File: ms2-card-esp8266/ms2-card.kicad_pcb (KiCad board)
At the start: 2 copper layers, 100 x 54 mm, 58 parts, among them J1 Schaltregler, J10 MicroSD_SPI_CD, J11 Conn_01x06, J2 ESP Prog, J20 Smartcard Connector, J21 PogoPin, J22 Card Edge, J23 Conn_01x04, J30 USB_B_Micro, J31 Power Select, J32 Conn_01x03, Q1 MMBT3904, Q2 MMBT3904, SW1 RESET, U1 ESP-12F, U2 FM24C64B, U20 BL1551B, U3 BL1551B, U30 CP2102N-Axx-xQFN24, U4 BL1551B, U6 AMS1117-3.3

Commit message: wip
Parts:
- moved D32 3.77 mm to (185.3, 151.8)
- moved R32 3.77 mm to (185.3, 150.1)
- moved D31 2.85 mm to (182.0, 151.8)
- moved R31 2.85 mm to (182.0, 150.1)
- moved R21 1.28 mm to (179.2, 138.5)
- moved R20 1.15 mm to (181.0, 138.5)
- turned D1 to 180 degrees
- turned R4 to 180 degrees
- turned R3 to 180 degrees
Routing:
- net VCC: track 0.00 -> 82.6 mm, vias 0 -> 2
- net /VBUS: track 14.3 -> 72.7 mm, vias 2 -> 3
- net Net-(J20-Pad4): track 0.00 -> 55.8 mm
- net Net-(J20-Pad5): track 0.00 -> 49.1 mm
- net /CS: track 0.00 -> 43.5 mm
- net /RxD: track 0.00 -> 38.3 mm
- net /TxD: track 0.00 -> 36.6 mm
- net /nRST: track 0.00 -> 29.7 mm, vias 0 -> 1
- net /MOSI: track 0.00 -> 29.4 mm
- net +5V: track 0.00 -> 25.6 mm, vias 0 -> 1
- net /RTS: track 0.00 -> 14.7 mm
- net /DTR: track 0.00 -> 14.1 mm, vias 0 -> 2
- net /CLK: track 0.00 -> 12.4 mm, vias 0 -> 2
- net /MISO: track 0.00 -> 10.5 mm
- net /LED: track 0.00 -> 8.85 mm
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
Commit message: in production
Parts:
- moved J23 0.14 mm to (160.4, 113.0)
- moved C2 0.11 mm to (167.1, 139.5)
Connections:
- U1 pad 22: unconnected-(U1-Pad22) -> /Card
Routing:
- net /CSCL: track 0.00 -> 96.5 mm, vias 0 -> 5
- net VCC: track 82.6 -> 170.5 mm, vias 2 -> 3
- net Net-(J22-Pad1): track 0.00 -> 81.3 mm
- net Net-(J20-Pad2): track 0.00 -> 73.6 mm
- net /CSDA: track 0.00 -> 68.9 mm, vias 0 -> 4
- net /MS2PWR: track 0.00 -> 65.0 mm
- net /PP: track 0.00 -> 61.3 mm, vias 0 -> 1
- net Net-(J20-Pad7): track 0.00 -> 49.4 mm
- net GND: track 9.67 -> 54.2 mm, vias 7 -> 25
- net /nRST: track 29.7 -> 67.7 mm
- net /I2C_SEL: track 0.00 -> 32.4 mm, vias 0 -> 1
- net /Card: track 0.00 -> 28.8 mm, vias 0 -> 1
- net /ESCL: track 6.93 -> 31.9 mm, vias 0 -> 4
- net /MSDA: track 0.00 -> 15.4 mm, vias 0 -> 2
- net /GPIO0: track 8.35 -> 21.4 mm, vias 1 -> 2
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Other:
- rule pad_to_mask_clearance: 0 -> 0.05

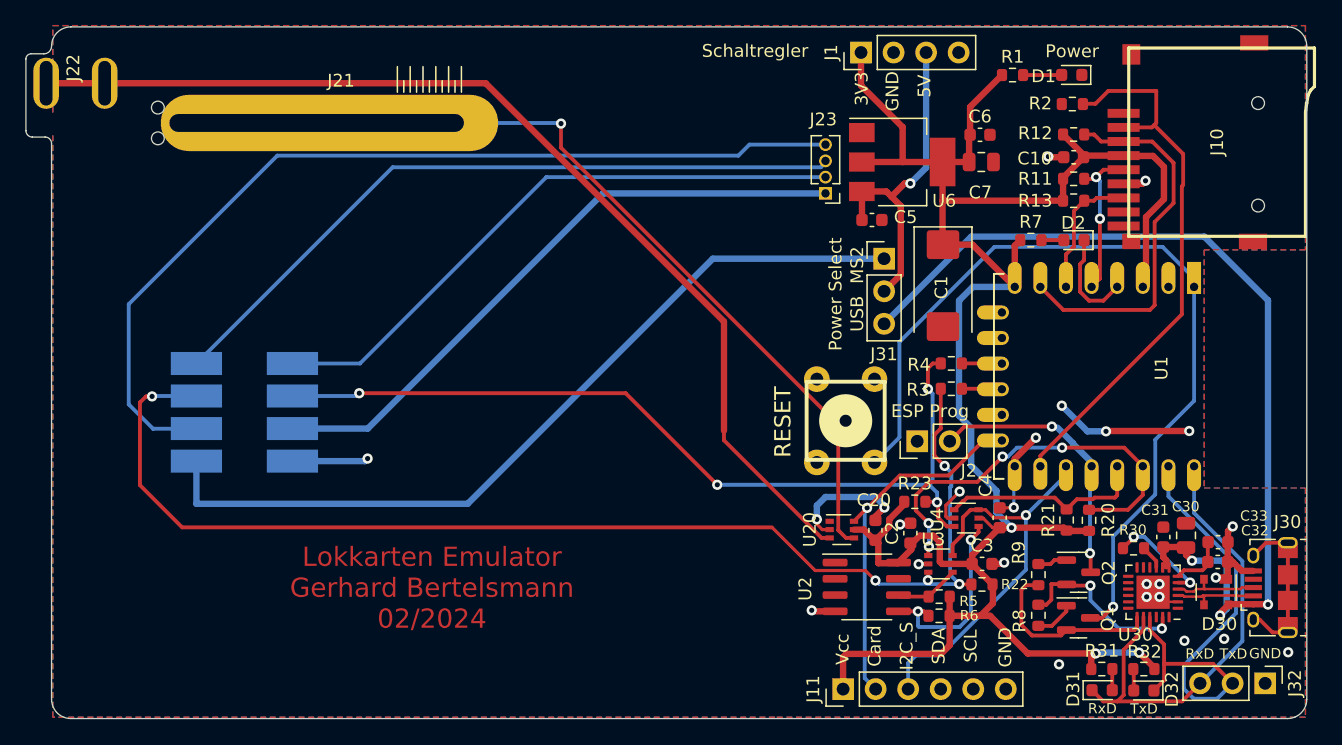
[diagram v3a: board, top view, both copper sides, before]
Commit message: replace SW1 / calm down DRC - part I
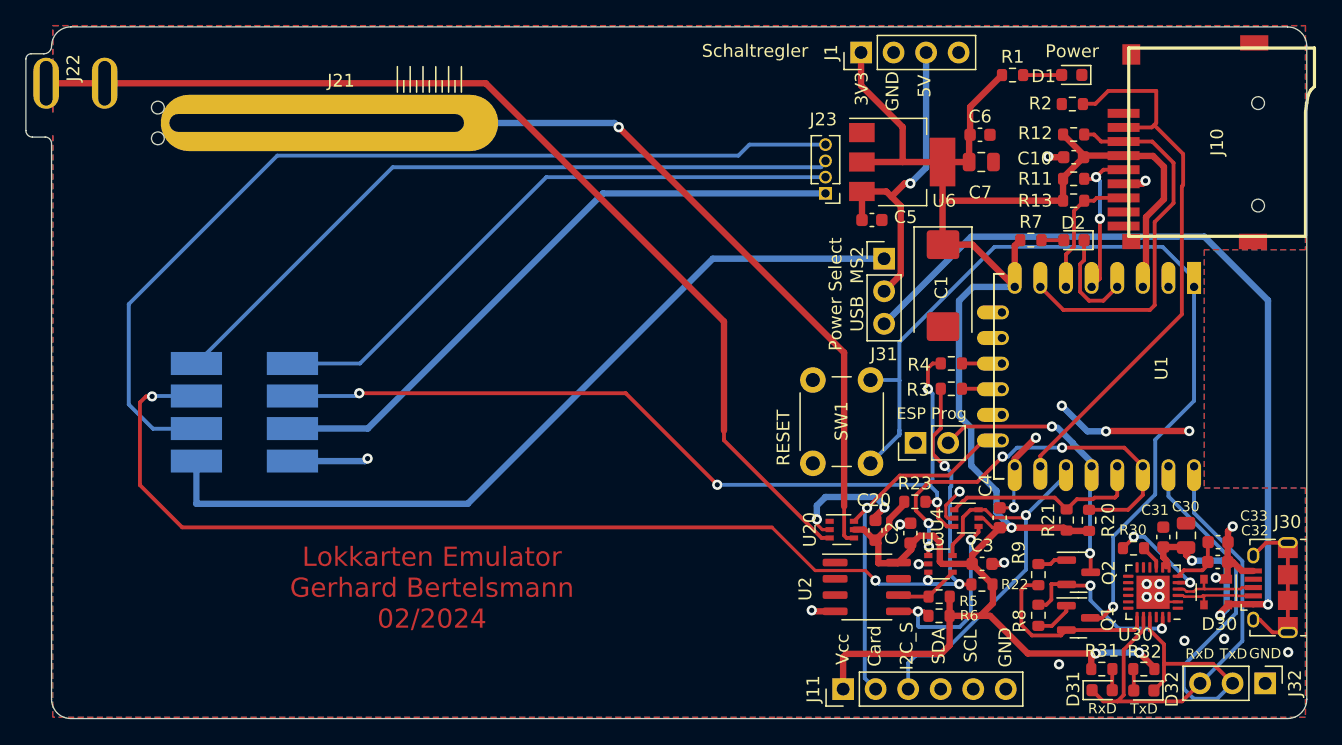
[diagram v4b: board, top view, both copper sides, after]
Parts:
- SW1: footprint w_switch:PCB_PUSH -> Button_Switch_THT:SW_PUSH_6mm_H4.3mm
- moved SW1 4.19 mm to (159.4, 134.1), turned to 90 degrees
- moved J2 0.18 mm to (167.5, 132.5)
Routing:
- net /nRST: track 67.7 -> 70.6 mm
- net /PP: track 61.3 -> 63.8 mm

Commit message: replace ESP8266 footprint with standard KiCAD
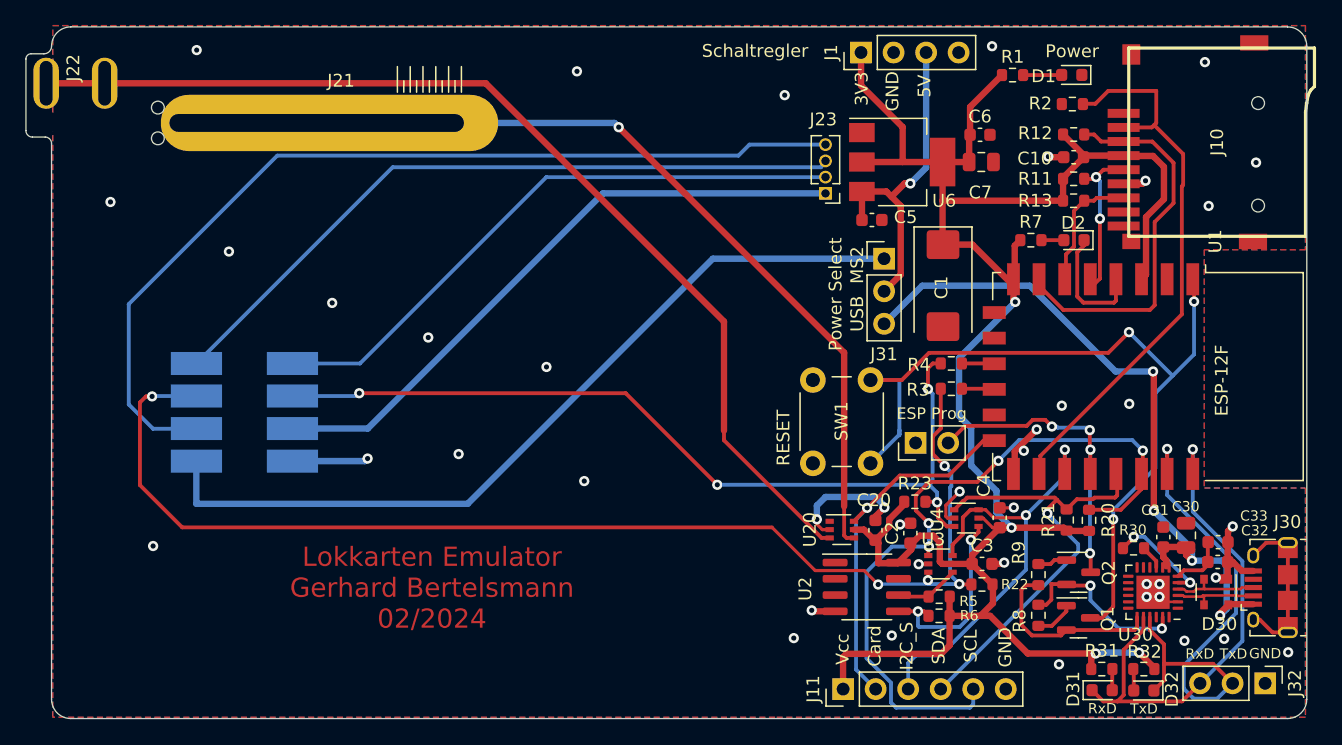
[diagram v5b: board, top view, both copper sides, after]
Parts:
- U1: footprint ESP8266:ESP-12E -> RF_Module:ESP-12E
- moved U1 7.87 mm to (185.6, 127.3)
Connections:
- J11 pad 4: /SDA -> /ESDA
- J11 pad 5: /SCL -> /ESCL
- U1 pad 10: /CS -> unconnected-(U1-Pad10)
- U1 pad 11: /I2C_SEL -> Net-(R4-Pad1)
- U1 pad 12: /GPIO0 -> Net-(R3-Pad1)
- U1 pad 13: /ESDA -> unconnected-(U1-Pad13)
- U1 pad 14: /ESCL -> /Card
- U1 pad 15: /RxD -> GND
- U1 pad 16: /TxD -> /CS
- U1 pad 17: unconnected-(U1-Pad17) -> /I2C_SEL
- U1 pad 18: unconnected-(U1-Pad18) -> /GPIO0
- U1 pad 19: Net-(R4-Pad1) -> /ESDA
- U1 pad 20: Net-(R3-Pad1) -> /ESCL
- U1 pad 21: unconnected-(U1-Pad21) -> /RxD
- U1 pad 22: /Card -> /TxD
- U1 pad 9: GND -> unconnected-(U1-Pad9)
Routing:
- net /ESCL: track 31.9 -> 57.4 mm
- net /ESDA: track 16.2 -> 36.8 mm, vias 0 -> 1
- net /VBUS: track 74.4 -> 55.7 mm, vias 3 -> 4
- net GND: track 54.2 -> 40.9 mm, vias 25 -> 42
- net /GPIO0: track 21.6 -> 25.2 mm, vias 2 -> 4
- net /nRST: track 70.6 -> 67.0 mm, vias 1 -> 3
- net /RxD: track 38.4 -> 41.7 mm, vias 0 -> 1
- net /TxD: track 36.7 -> 40.0 mm, vias 0 -> 1
- net /I2C_SEL: track 32.4 -> 35.6 mm, vias 1 -> 2
- net VCC: track 170.5 -> 168.7 mm, vias 3 -> 4
- net /LED: track 7.79 -> 9.58 mm
- net Net-(R4-Pad1): track 3.13 -> 2.54 mm
- net Net-(R3-Pad1): track 3.14 -> 2.55 mm
- net /Card: track 28.8 -> 29.3 mm

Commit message: fix SD CARD DRC check
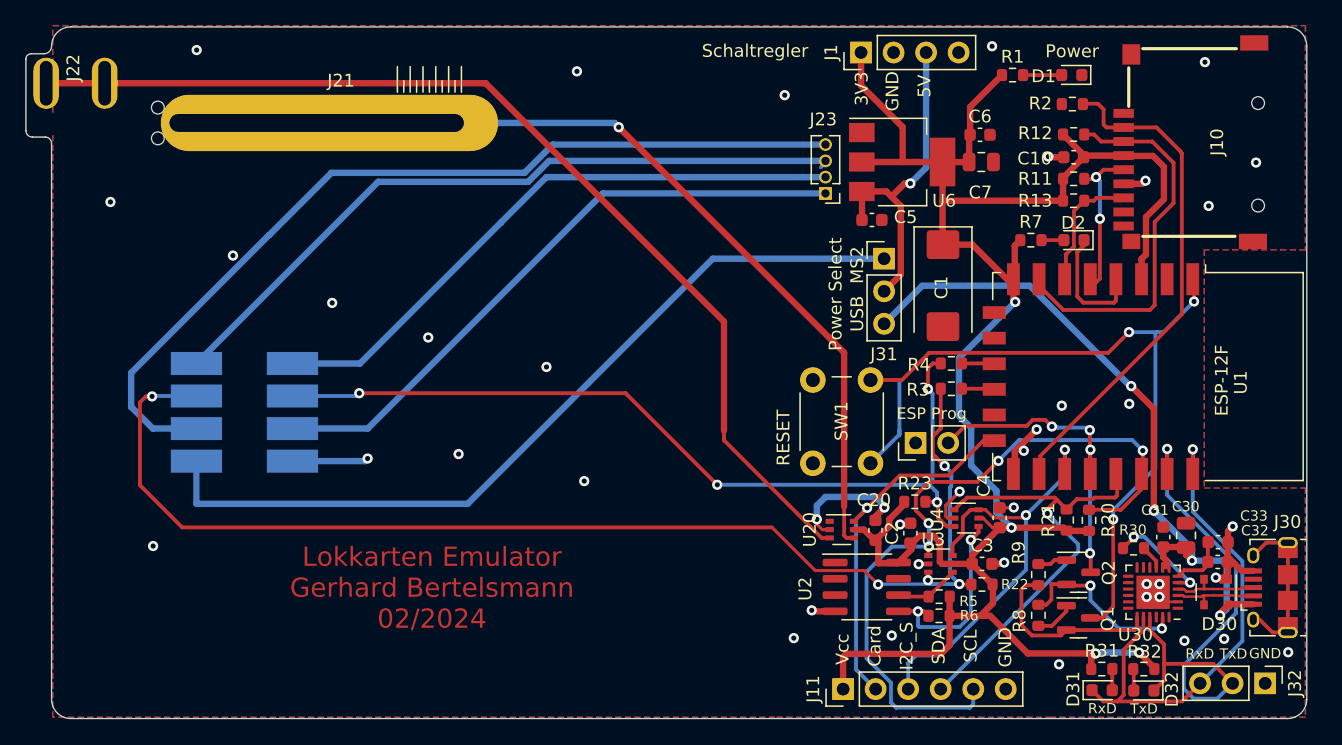
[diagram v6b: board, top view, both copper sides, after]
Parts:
- J10: footprint w_conn_misc:GCT-MEM2055-00-190-01-A -> sd-card-conn:GCT-MEM2055-00-190-01-A
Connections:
- J10 pad 1: (no net) -> unconnected-(J10-Pad1)
- J10 pad 10: (no net) -> unconnected-(J10-Pad10)
- J10 pad 8: (no net) -> unconnected-(J10-Pad8)
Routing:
- net Net-(J20-Pad5): track 47.8 -> 69.6 mm
- net Net-(J20-Pad2): track 73.6 -> 91.5 mm
- net /CS: track 43.5 -> 39.1 mm
- net /nRST: track 67.0 -> 64.7 mm
- net /VBUS: track 55.7 -> 54.0 mm
- net Net-(J20-Pad4): track 55.8 -> 56.4 mm

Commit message: minor changes
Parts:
- moved J31 5.10 mm to (164.8, 123.2), turned to 180 degrees
- moved C7 2.25 mm to (172.6, 112.8)
- moved C6 2.21 mm to (172.4, 110.6)
- moved C5 1.52 mm to (162.5, 115.1), turned to 180 degrees
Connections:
- C5 pad 1: +5V -> /VBUS
- C6 pad 1: VCC -> +3V3
- C7 pad 1: VCC -> +3V3
- J1 pad 3: +5V -> /VBUS
- J31 pad 2: +5V -> VCC
- J31 pad 3: /VBUS -> +3V3
- U6 pad 2: VCC -> +3V3
- U6 pad 3: +5V -> /VBUS
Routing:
- net +5V: track 25.6 -> 0.00 mm, vias 1 -> 0
- net +3V3: track 0.00 -> 19.1 mm
- net /VBUS: track 54.0 -> 70.7 mm, vias 4 -> 5
- net VCC: track 168.7 -> 158.8 mm
- net /MS2PWR: track 65.0 -> 62.6 mm
- net Net-(J20-Pad4): track 56.4 -> 55.7 mm

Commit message: wip
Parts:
- removed D2: LED, LED_SMD:LED_0603_1608Metric
- removed R7: 330, Resistor_SMD:R_0603_1608Metric
- R3: value 0 -> 220K
- R4: value 0 -> 100K
- moved R4 13.4 mm to (179.4, 116.5)
- moved R3 12.8 mm to (175.4, 116.5), turned to 0 degrees
- moved SW1 1.69 mm to (161.1, 133.6)
- moved J2 1.57 mm to (169.0, 132.8), turned to 180 degrees
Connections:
- R3 pad 1: Net-(R3-Pad1) -> /CSCL
- R3 pad 2: /CSCL -> Net-(U1-Pad2)
- R4 pad 1: Net-(R4-Pad1) -> GND
- R4 pad 2: /CSDA -> Net-(U1-Pad2)
- U1 pad 11: Net-(R4-Pad1) -> unconnected-(U1-Pad11)
- U1 pad 12: Net-(R3-Pad1) -> unconnected-(U1-Pad12)
- U1 pad 14: /Card -> unconnected-(U1-Pad14)
- U1 pad 2: unconnected-(U1-Pad2) -> Net-(U1-Pad2)
- U1 pad 4: /LED -> /Card
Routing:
- net /Card: track 29.3 -> 46.0 mm, vias 1 -> 3
- net GND: track 40.9 -> 56.9 mm, vias 42 -> 47
- net Net-(U1-Pad2): track 0.00 -> 14.3 mm, vias 0 -> 2
- net /CSCL: track 96.7 -> 110.2 mm
- net /MOSI: track 29.4 -> 16.4 mm, vias 0 -> 2
- net /CSDA: track 68.9 -> 58.4 mm, vias 4 -> 3
- net /LED: track 9.58 -> 0.00 mm
- net /nRST: track 64.7 -> 59.3 mm
- net Net-(R3-Pad1): track 2.55 -> 0.00 mm
- net Net-(R4-Pad1): track 2.54 -> 0.00 mm
- net Net-(D2-Pad2): track 1.75 -> 0.00 mm
- net /GPIO0: track 25.2 -> 26.2 mm
- net /CLK: track 12.4 -> 11.8 mm
- net /MISO: track 10.5 -> 9.93 mm
